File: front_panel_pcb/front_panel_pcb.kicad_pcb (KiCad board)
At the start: 2 copper layers, 93.3 x 100 mm, 41 parts

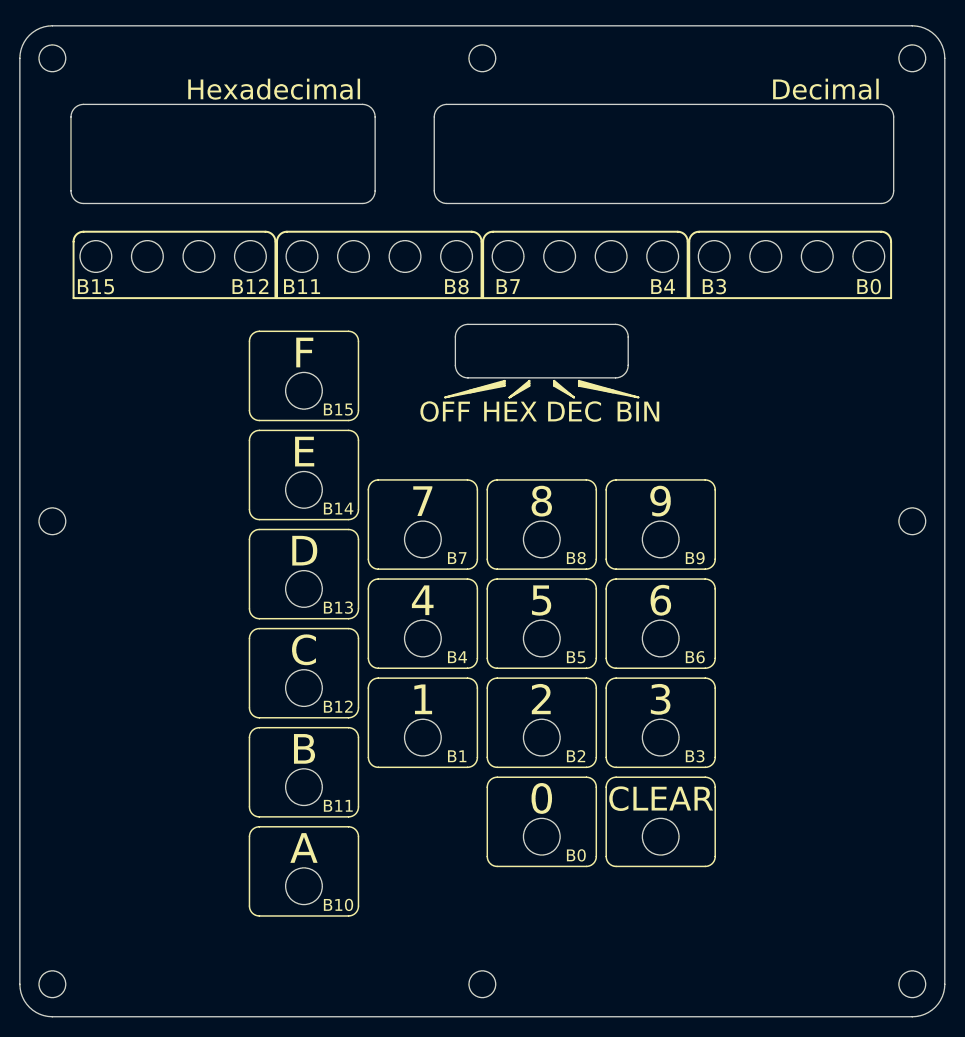
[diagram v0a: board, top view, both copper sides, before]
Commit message: pretty front silscreen
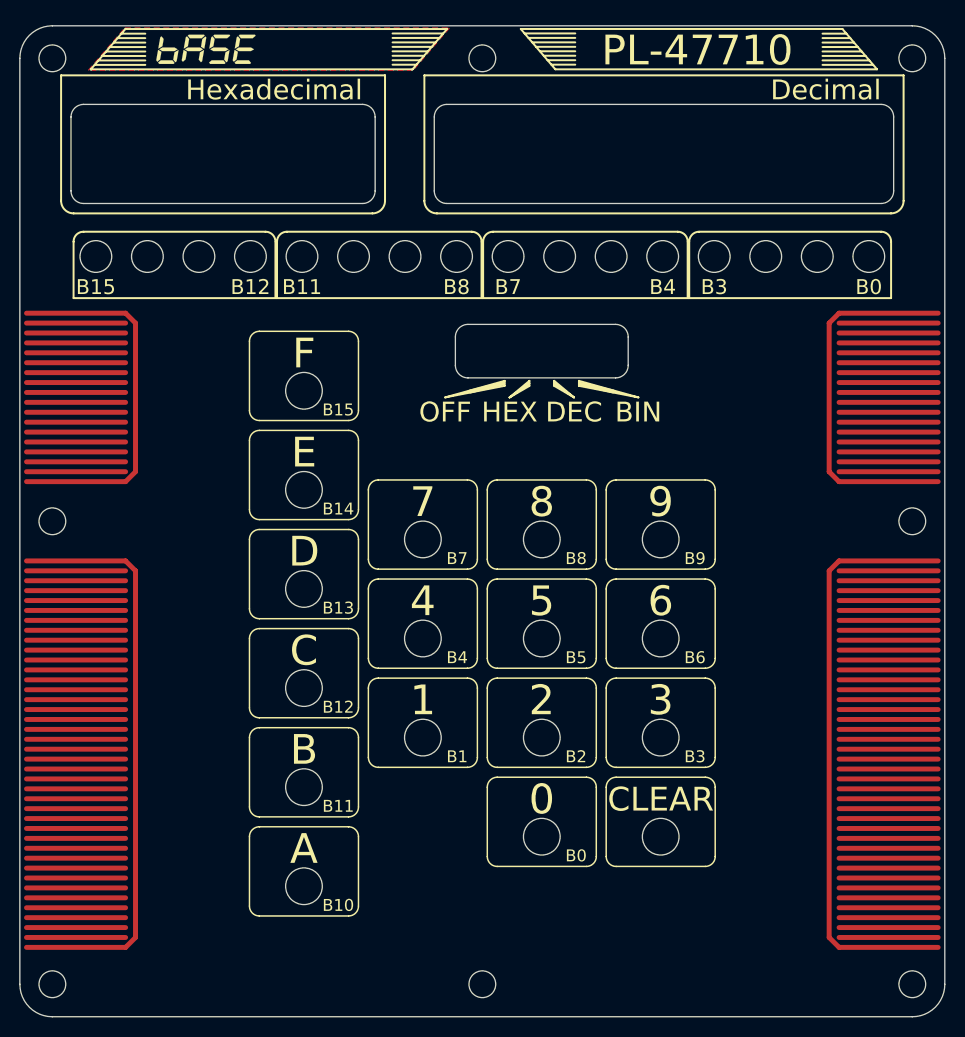
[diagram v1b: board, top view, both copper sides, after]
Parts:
- added G***: LOGO, Artwork:base_7segFontMissingSegs_Height-3mm, F.Cu at (72.2, 52.4)
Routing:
- net (no net): track 0.00 -> 1275.3 mm
- added copper zone on F.Cu, net (none)
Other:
- board text added: "CONVERT"
- board text added: "PL-47710"

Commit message: copper flood back and front, adjust some things
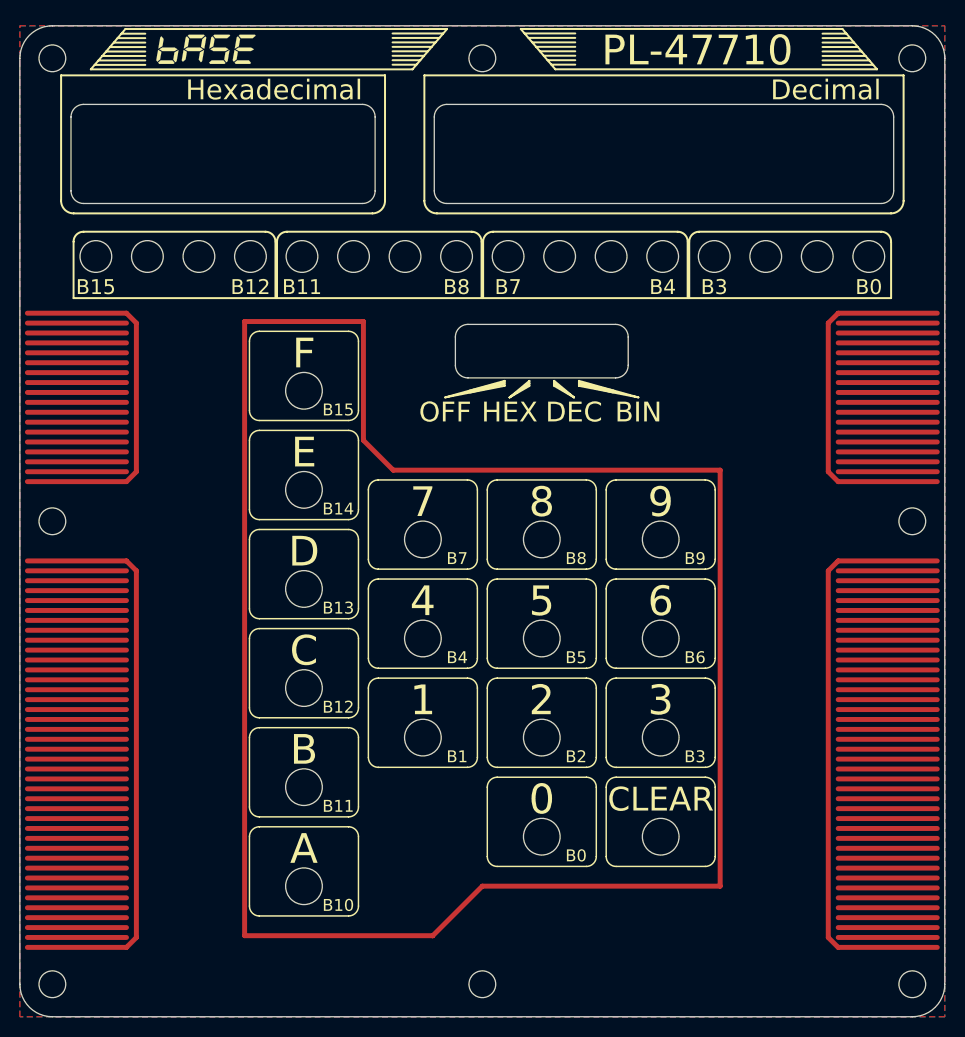
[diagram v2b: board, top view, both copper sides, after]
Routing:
- net (no net): track 1275.3 -> 1490.6 mm
- added copper zone on B.Cu, net (none)
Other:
- board text added: "Base Convert Front Panel PCB github.com/sdp8483/base_convert Sam Perry July 2018"

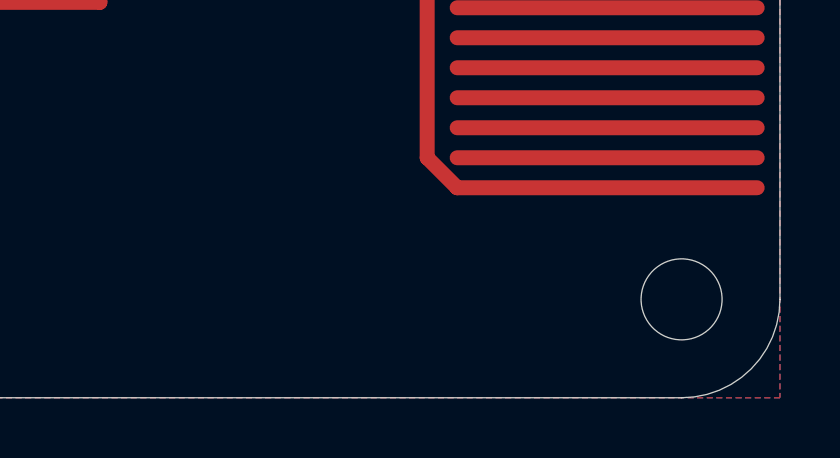
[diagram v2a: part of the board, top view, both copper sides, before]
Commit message: add logo
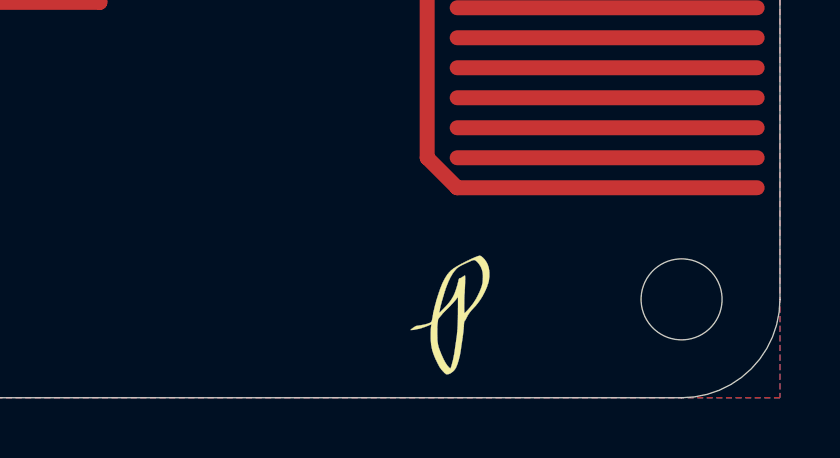
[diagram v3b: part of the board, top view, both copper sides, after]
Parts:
- added G***: LOGO, PL_logo:logo_height_20mm, B.Cu at (133.2, 106.5)
- added G***: LOGO, PL_logo:logo_height_4mm, F.Cu at (135.7, 147.2)
